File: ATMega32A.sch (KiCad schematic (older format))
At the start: 18 parts, among them J301 UART, J302 AVR-ISP-6, U301 ATmega32A-AU, Y301 16MHz

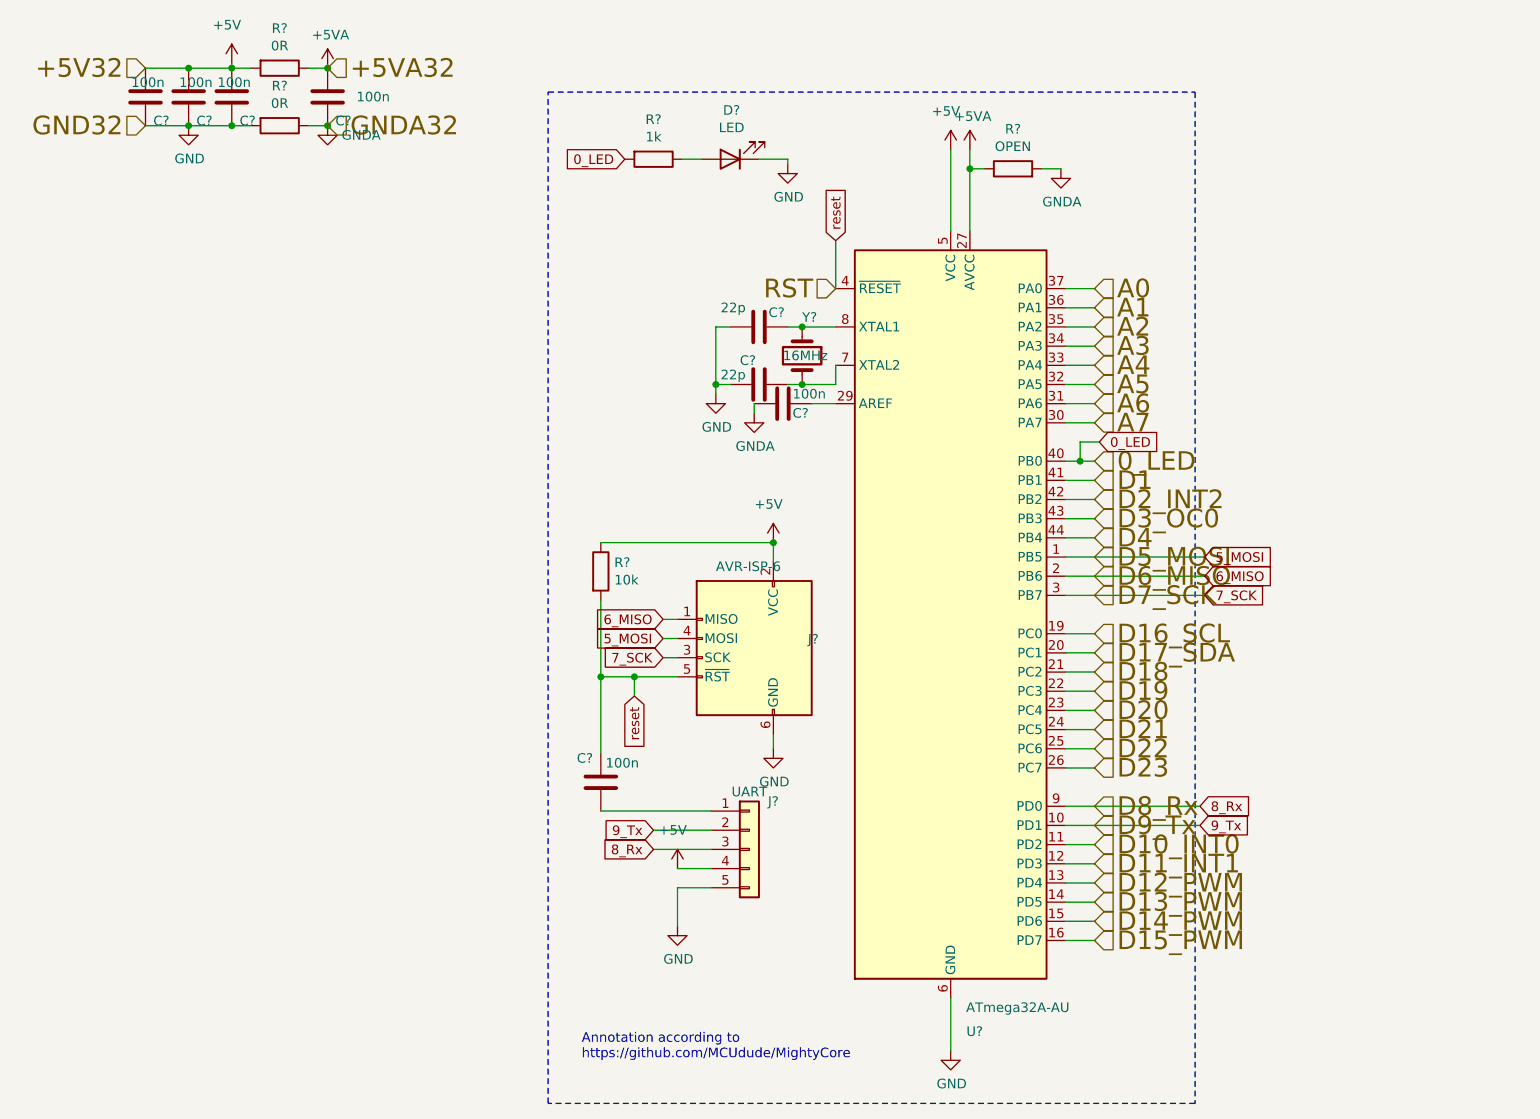
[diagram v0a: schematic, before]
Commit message: annotate dac
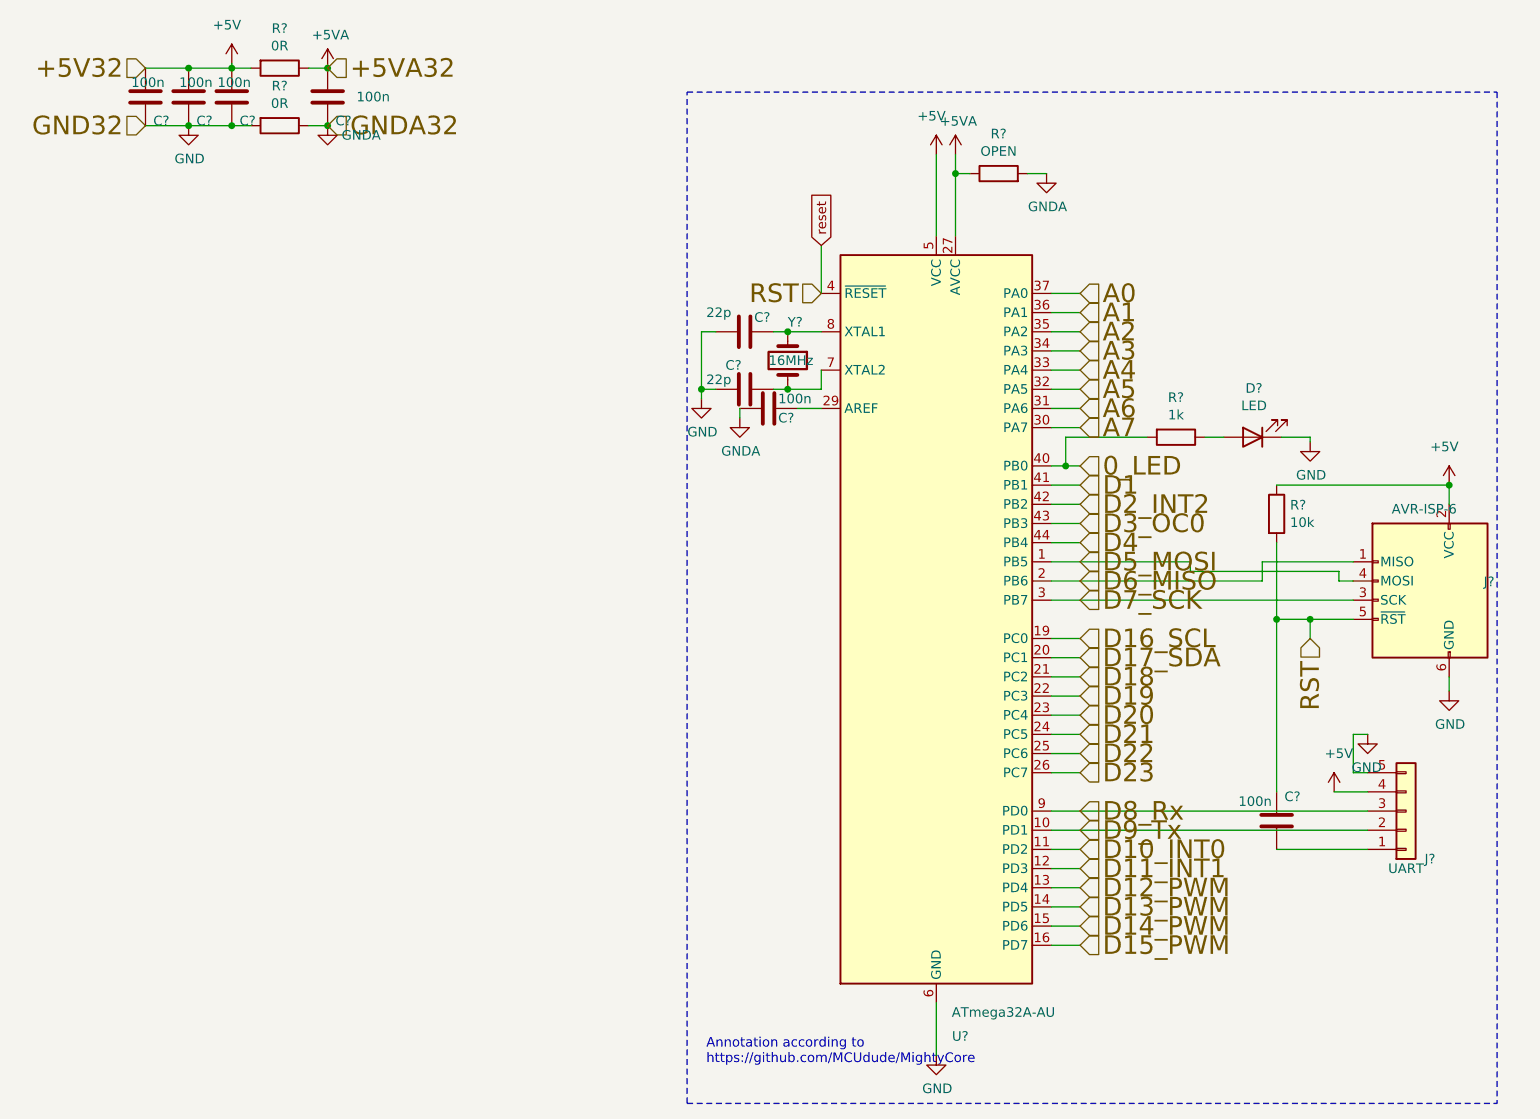
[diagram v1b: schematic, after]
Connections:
- net 5_MOSI renamed D5_MOSI
- net 6_MISO renamed D6_MISO
- net 7_SCK renamed D7_SCK
- net 8_Rx renamed D8_Rx
- net 9_Tx renamed D9_Tx
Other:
- moved on the sheet: C?, D?, J?, R?, U?, Y?

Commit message: footprints dac
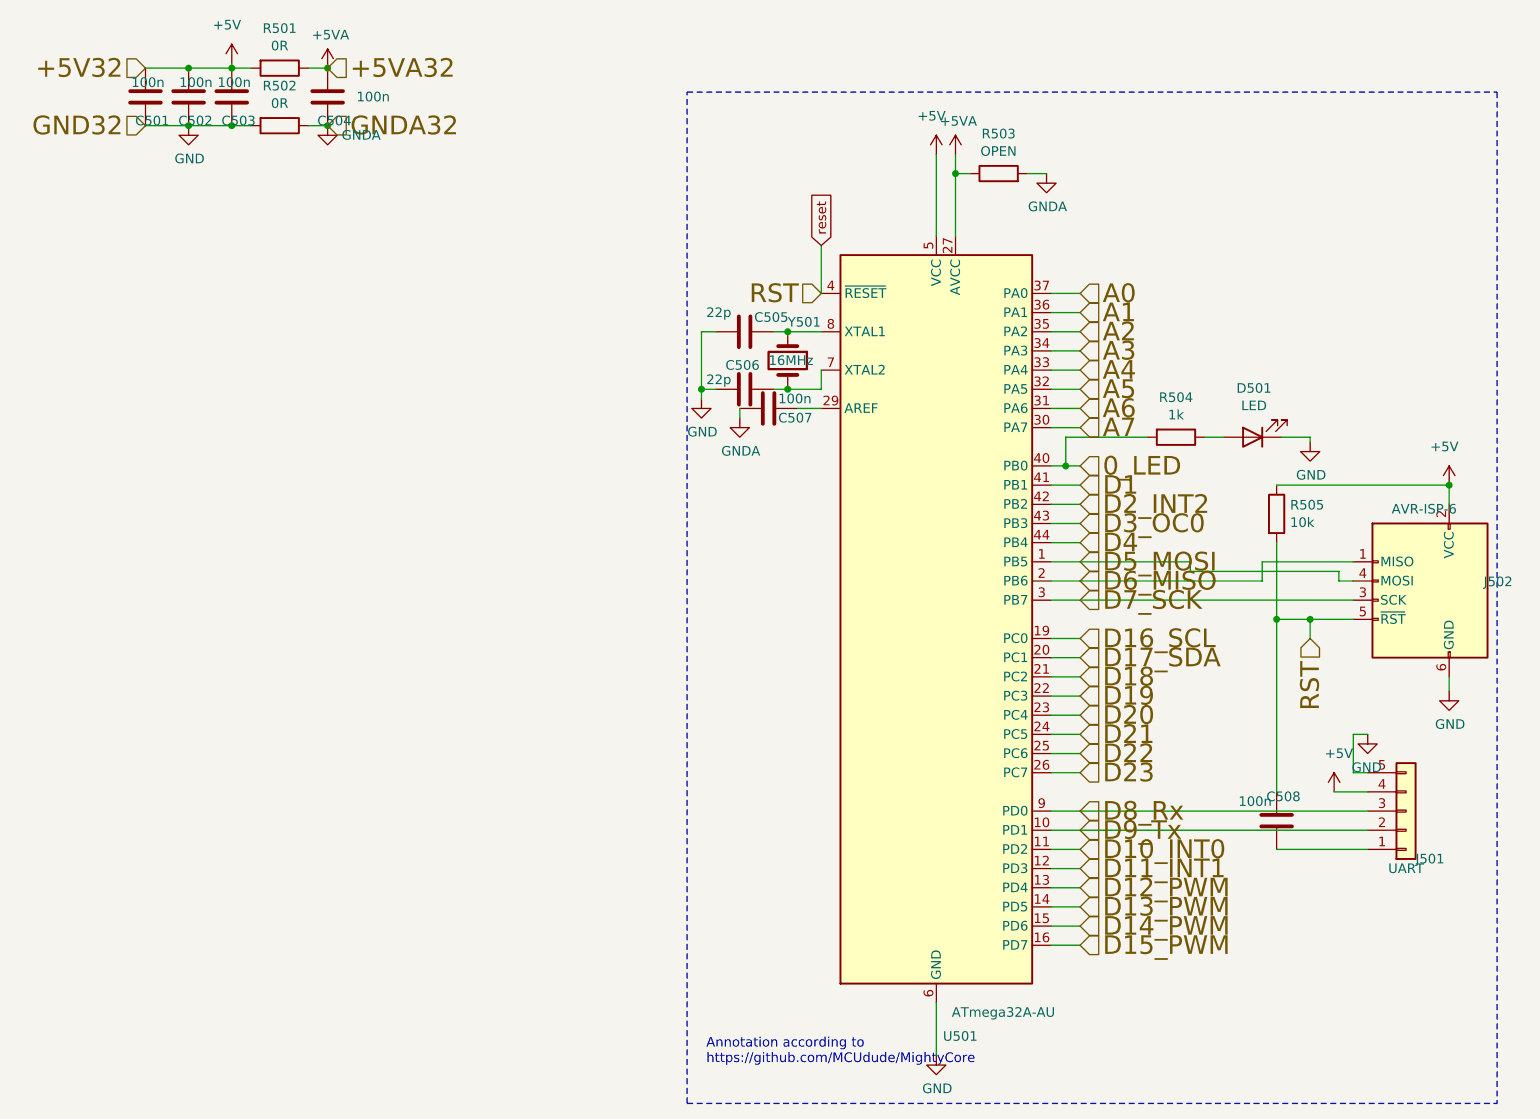
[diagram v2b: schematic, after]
